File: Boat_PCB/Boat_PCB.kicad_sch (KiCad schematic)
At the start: 41 parts, among them J1 Conn_02x06_Odd_Even, J11 Temp + Humidity Sensor Extern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, J12 led GPIO 12, J13 Temp + Humidity Sensor Intern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, J14 Conn_01x20_Socket, J15 Hull Leak Right GPIO 20, J16 Hull Leak Left GPIO 19, J17 Conn_01x20_Socket, J18 Stepper Motor, J2 Conn_01x03_Socket, J3 Raspberry Pi 5 connector, J4 12s Tap, J5 IMU 14,15 I2C 17,18 RST and I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, J6 4s output, J7 GPS + Compass GPIO 8,9 +15,14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, J8 Winch ESC GPIO 21, J9 Winch ESC RC, U1 MCP2515-I_P, U2 TJA1051T-3, Y1 Crystal

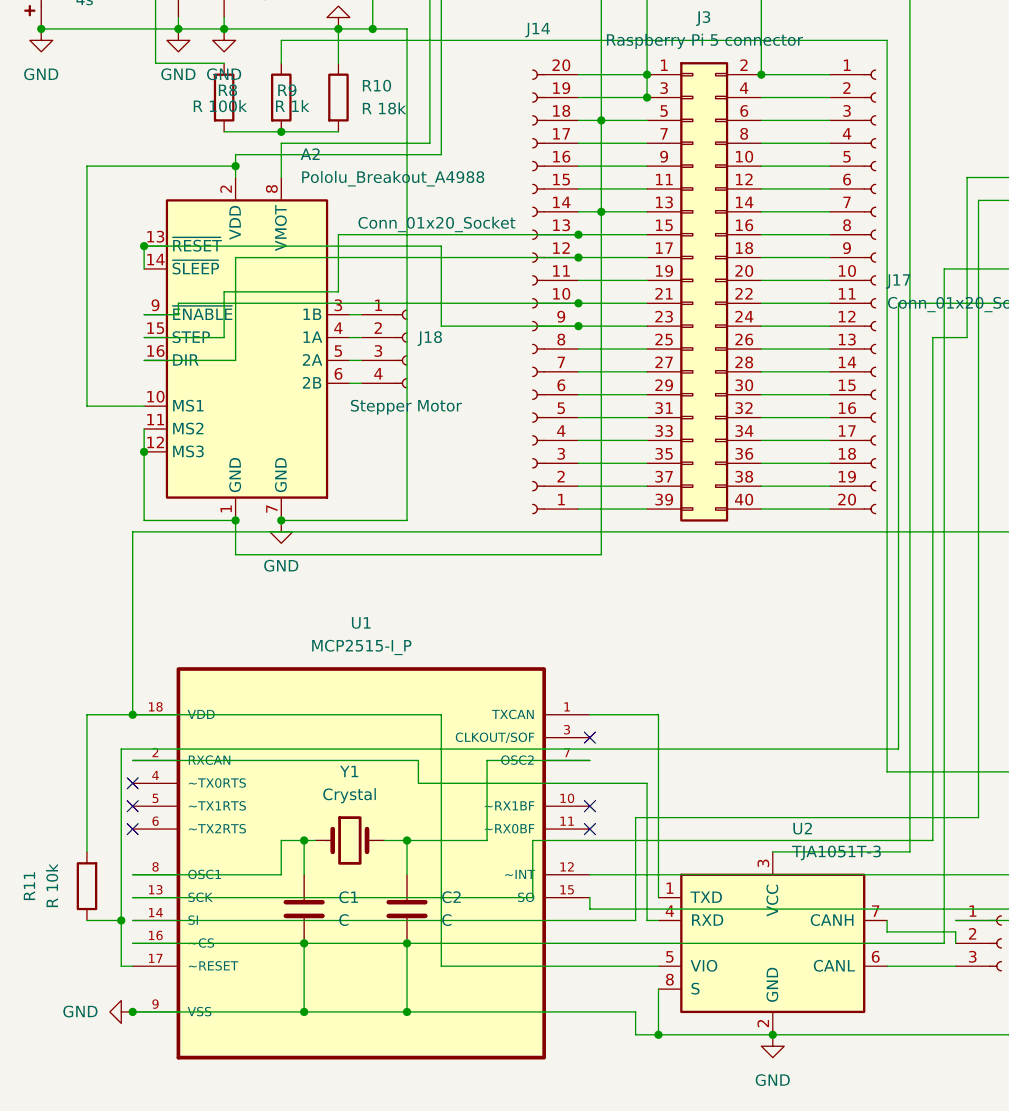
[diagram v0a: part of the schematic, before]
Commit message: Add three-tier survey vision pipeline with threat tracking
Layers a cheap water-segmentation anomaly screen (Tier 1) in front of
the existing YOLO overlay (Tier 2, now gated on anomaly), plus a threat
assessor (Tier 3) that turns detections into distance/approach-vector
radar tracking and mission alerts. Adds config, tests, and updates the
command center UI and hardware runner to wire it in. Also captures the
KiCad schematic/PCB updates from the M18 battery migration and refreshes
the session journal.
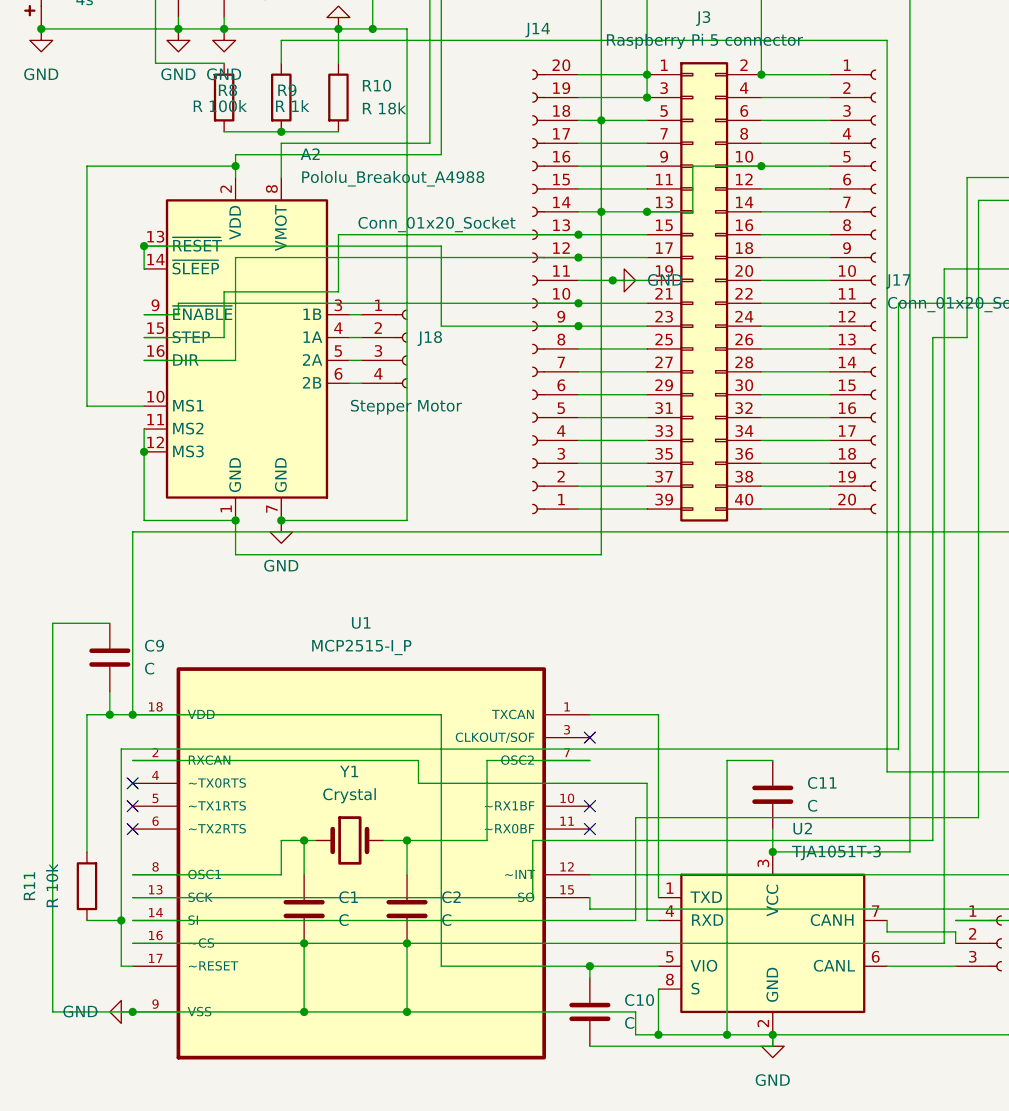
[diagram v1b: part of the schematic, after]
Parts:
- added C10, C11, C9: C, Capacitor_THT:C_Disc_D5.0mm_W2.5mm_P5.00mm, symbol Device:C
- C5, C7: footprint Capacitor_THT:CP_Radial_D8.0mm_P3.50mm -> Capacitor_THT:CP_Radial_D10.0mm_P5.00mm
- J13: footprint Connector_JST:JST_XH_B4B-XH-A_1x04_P2.50mm_Vertical -> Connector_PinHeader_2.54mm:PinHeader_1x04_P2.54mm_Vertical
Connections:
- net GND: now also J14.11 (Pin_11), J17.5 (Pin_5), J3.10 (Pin_10), J3.19 (Pin_19), C10.2, C11.1, C9.1
- net at A1.36 (3V3), J5.1 (Pin_1), R11.2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: now also C10.1, C9.2
- net at A1.39 (VSYS), J1.1 (Pin_1), J1.2 (Pin_2)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: now also C11.2
